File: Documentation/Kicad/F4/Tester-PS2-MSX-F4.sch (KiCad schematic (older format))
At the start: 3 parts, among them Q1 2SC1815, U1 WeAct Studio STM32F401CEU6 V3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

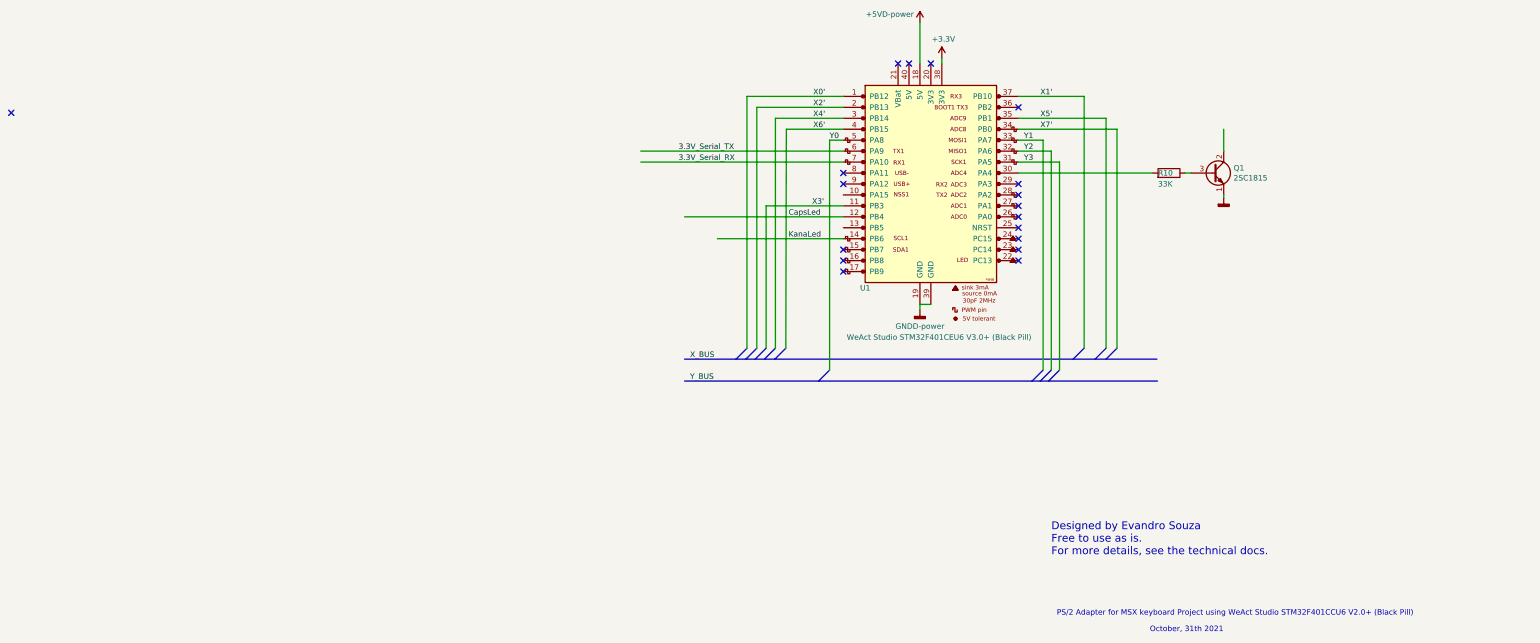
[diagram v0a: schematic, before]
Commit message: Add timing port function
Update F4 and F1 documentation
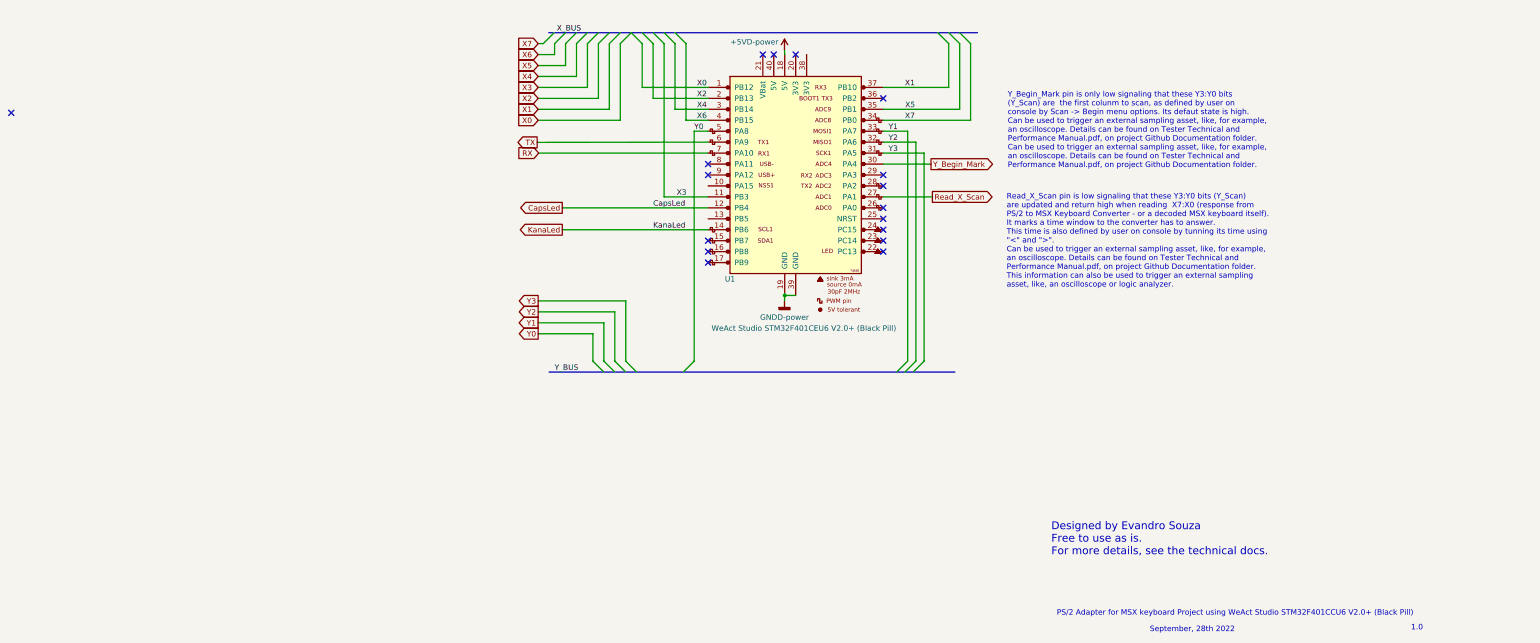
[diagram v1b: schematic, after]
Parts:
- removed Q1: 2SC1815, Package_TO_SOT_THT:TO-92_Inline, symbol Tester-PS2-MSX-F4-rescue:2SC1815-Transistor_BJT-PS2-MSX-F4-rescue-PS2-MSX-F4-re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
- removed R10: 33K, Resistor_THT:R_Axial_DIN0204_L3.6mm_D1.6mm_P7.62mm_Horizontal, symbol Tester-PS2-MSX-F4-rescue:R-Device-PS2-MSX-F4-rescue-PS2-MSX-F4-rescue
- U1: value WeAct Studio STM32F401CEU6 V3.0+ (Black Pill) -> WeAct Studio STM32F401CEU6 V2.0+ (Black Pill)
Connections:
- net labels added: RX, Read_X_Scan, TX, X0, X1, X2, X3, X4, X5, X6, X7, Y_Begin_Mark
- net labels removed: +3.3V, 3.3V_Serial_RX, 3.3V_Serial_TX, X0', X1', X2', X3', X4', X5', X6', X7'
- wire segments 36 -> 56
- no-connect marks 18 -> 17
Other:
- note added: "1.0"
- note added: "Read_X_Scan pin is low signaling that these Y3:Y0 bits (Y_Scan)\nare updated and return high when reading X7:X0 (response from\nPS/2 to MSX Keyboard Converter - or a decoded MSX keyboard itself).\nIt marks a time window to the converter has to answer.\nThis time is also defined by user on console by tunning its time using\n"<" and ">".\nCan be used to trigger an external sampling asset, like, for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"
- note added: "September, 28th 2022"
- note added: "Y_Begin_Mark pin is only low signaling that these Y3:Y0 bits\n(Y_Scan) are the first colunm to scan, as defined by user on\nconsole by Scan -> Begin menu options. Its defaut state is high.\nCan be used to trigger an external sampling asset, like, for example,\nan oscilloscope. Details can be found on Tester Technical and\nPerformance Manual.pdf, on project Github Documentation folder.\nCan be use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"
- note removed: "October, 31th 2021"
- moved on the sheet: U1

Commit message: Update Kicad files
Update F4 and F1 Kicad documentation
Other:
- note added: "Read_X_Scan pin is low signaling that these Y3:Y0 bits (Y_Scan)\nare updated and return high when reading X7:X0 (response from\nPS/2 to MSX Keyboard Converter - or a decoded MSX keyboard itself).\n\nIt marks a time window to the converter has to answer.\nThis time is also defined by user on console by tunning its time using\n"<" and ">".\n\nThis information can also be used to trigger an external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"
- note added: "Y_Begin_Mark pin is only low signaling that these Y3:Y0 bits\n(Y_Scan) are the first colunm to scan, as defined by user on\nconsole by Scan -> Begin menu options. Its defaut state is high.\n\nCan be used to trigger an external sampling asset, like, for example,\nan oscilloscope."
- note removed: "Read_X_Scan pin is low signaling that these Y3:Y0 bits (Y_Scan)\nare updated and return high when reading X7:X0 (response from\nPS/2 to MSX Keyboard Converter - or a decoded MSX keyboard itself).\nIt marks a time window to the converter has to answer.\nThis time is also defined by user on console by tunning its time using\n"<" and ">".\nCan be used to trigger an external sampling asset, like, for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"
- note removed: "Y_Begin_Mark pin is only low signaling that these Y3:Y0 bits\n(Y_Scan) are the first colunm to scan, as defined by user on\nconsole by Scan -> Begin menu options. Its defaut state is high.\nCan be used to trigger an external sampling asset, like, for example,\nan oscilloscope. Details can be found on Tester Technical and\nPerformance Manual.pdf, on project Github Documentation folder.\nCan be use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"
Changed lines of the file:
@@
 Wire Wire Line
 	3413 2968 2663 2968
-Text Notes 6952 3411 0    50   ~ 0
-Y_Begin_Mark pin is only low signaling that these Y3:Y0 bits\n(Y_Scan) are  the first colunm to scan, as defined by user on\nconsole by Scan -> Begin menu options. Its defaut state is high.\nCan be used to trigger an external sampling asset, like, for example,\nan oscilloscope. Details can be found on Tester Technical and\nPerformance Manual.pdf, on project Github Documentation folder.\nCan be used to trigger an external sampling asset, like, for example,\nan oscilloscope. Details can be found on Tester Technical and\nPerformance Manual.pdf, on project Github Documentation folder.
-Text Notes 6942 4503 0    50   ~ 0
-Read_X_Scan pin is low signaling that these Y3:Y0 bits (Y_Scan)\nare updated and return high when reading  X7:X0 (response from\nPS/2 to MSX Keyboard Converter - or a decoded MSX keyboard itself).\nIt marks a time window to the converter has to answer.\nThis time is also defined by user on console by tunning its time using\n"<" and ">".\nCan be used to trigger an external sampling asset, like, for example,\nan oscilloscope. Details can be found on Tester Technical and\nPerformance Manual.pdf, on project Github Documentation folder.\nThis information can also be used to trigger an external sampling\nasset, like, an oscilloscope or logic analyzer.
+Text Notes 6938 3501 0    50   ~ 0
+Y_Begin_Mark pin is only low signaling that these Y3:Y0 bits\n(Y_Scan) are  the first colunm to scan, as defined by user on\nconsole by Scan -> Begin menu options. Its defaut state is high.\n\nCan be used to trigger an external sampling asset, like, for example,\nan oscilloscope.
+Text Notes 6946 4657 0    50   ~ 0
+Read_X_Scan pin is low signaling that these Y3:Y0 bits (Y_Scan)\nare updated and return high when reading  X7:X0 (response from\nPS/2 to MSX Keyboard Converter - or a decoded MSX keyboard itself).\n\nIt marks a time window to the converter has to answer.\nThis time is also defined by user on console by tunning its time using\n"<" and ">".\n\nThis information can also be used to trigger an external\nsampling asset, like, an oscilloscope or logic analyzer.\n\nDetails can be found on the pdf file Tester Technical and \nPerformance Manual, on project Github Documentation folder.
 Text Notes 10636 7634 0    50   ~ 0
 1.0
